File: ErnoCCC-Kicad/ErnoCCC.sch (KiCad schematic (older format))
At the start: 81 parts, among them J1 6VAC, J2 ICSP, J3 FTDI, J4 Erno Controller, J5 SWITCH, J6 LED OUT, J7 Conn_01x05, Q1 BC847, Q2 BC847, SW1 SW_Push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

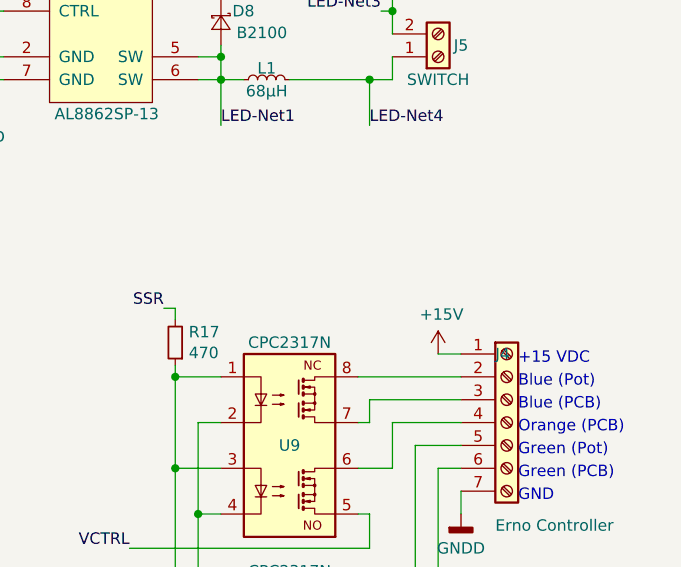
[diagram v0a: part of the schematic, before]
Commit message: Adding a 15VDC Elko
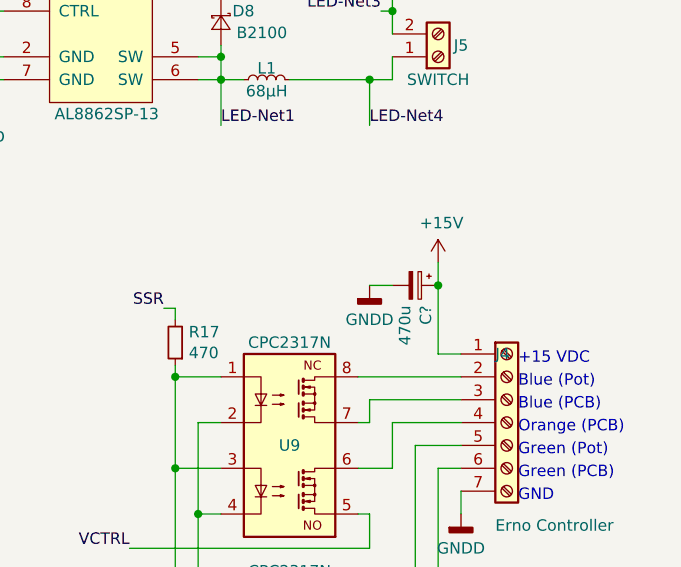
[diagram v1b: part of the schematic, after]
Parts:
- added C?: 470u, Capacitor_SMD:CP_Elec_10x10, symbol Device:CP_Small
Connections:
- wire segments 310 -> 313
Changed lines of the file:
@@
 Text Notes 10400 3850 0    50   ~ 0
 GND
-$Comp
-L power:+15V #PWR032
-U 1 1 5E443EB7
-P 10050 3200
-F 0 "#PWR032" H 10050 3050 50  0001 C CNN
-F 1 "+15V" H 10065 3373 50  0000 C CNN
-F 2 "" H 10050 3200 50  0001 C CNN
-F 3 "" H 10050 3200 50  0001 C CNN
-	1    10050 3200
-	1    0    0    -1
-$EndComp
 Text Notes 10400 3750 0    50   ~ 0
 Green (PCB)
@@
 Wire Wire Line
 	5600 4900 5700 4900
+$Comp
+L Device:CP_Small C?
+U 1 1 5E1CEF91
+P 9950 2900
+F 0 "C?" H 10038 2946 50  0000 L CNN
+F 1 "470u" H 10038 2855 50  0000 L CNN
+F 2 "Capacitor_SMD:CP_Elec_10x10" H 9950 2900 50  0001 C CNN
+F 3 "https://www.mouser.de/datasheet/2/293/e-wd-1511808.pdf" H 9950 2900 50  0001 C CNN
+	1    9950 2900
+	0    1    1    0
+$EndComp
+$Comp
+L power:+15V #PWR032
+U 1 1 5E443EB7
+P 10050 2800
+F 0 "#PWR032" H 10050 2650 50  0001 C CNN
+F 1 "+15V" H 10065 2973 50  0000 C CNN
+F 2 "" H 10050 2800 50  0001 C CNN
+F 3 "" H 10050 2800 50  0001 C CNN
+	1    10050 2800
+	1    0    0    -1
+$EndComp
+$Comp
+L power:GNDD #PWR?
+U 1 1 5E1D39DC
+P 9750 2900
+F 0 "#PWR?" H 9750 2650 50  0001 C CNN
+F 1 "GNDD" H 9750 2750 50  0000 C CNN
+F 2 "" H 9750 2900 50  0001 C CNN
+F 3 "" H 9750 2900 50  0001 C CNN
+	1    9750 2900
+	1    0    0    -1
+$EndComp
+Wire Wire Line
+	9750 2900 9850 2900
+Wire Wire Line
+	10050 2900 10050 3200
+Wire Wire Line
+	10050 2800 10050 2900
+Connection ~ 10050 2900
 $EndSCHEMATC

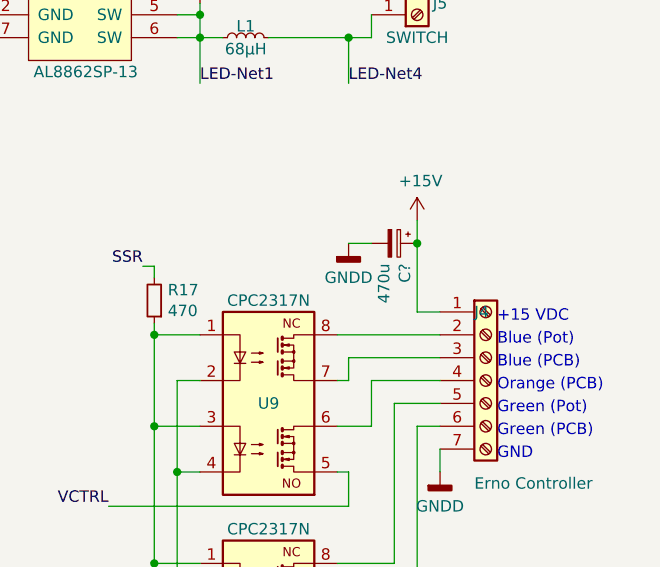
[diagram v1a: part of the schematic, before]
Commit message: Updating the Pin Header Length (6x done, 4x and 7x to follow)
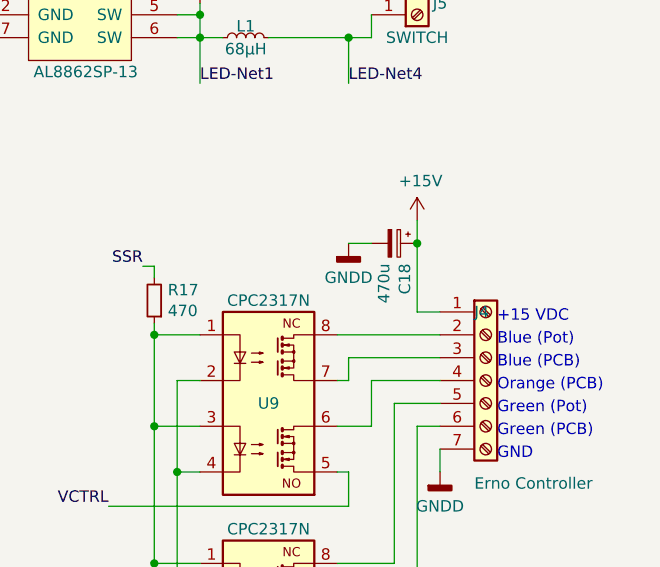
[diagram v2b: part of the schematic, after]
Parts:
- C12, C15: footprint Capacitor_SMD:CP_Elec_5x5.8 -> Capacitor_SMD:CP_Elec_4x4.5
- J3: footprint Connector_PinHeader_2.54mm:PinHeader_1x06_P2.54mm_Horizontal -> Connector_PinHeader_2.54mm:PinHeader_1x06_P2.54mm_Horizontal_shorter
- gave numbers to parts that had none: 1
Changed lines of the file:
@@
 F 0 "J3" H 4830 4592 50  0000 L CNN
 F 1 "FTDI" H 4750 4200 50  0000 L CNN
-F 2 "Connector_PinHeader_2.54mm:PinHeader_1x06_P2.54mm_Horizontal" H 4750 4600 50  0001 C CNN
+F 2 "Connector_PinHeader_2.54mm:PinHeader_1x06_P2.54mm_Horizontal_shorter" H 4750 4600 50  0001 C CNN
 F 3 "~" H 4750 4600 50  0001 C CNN
 	1    4750 4600
@@
 F 0 "C12" H 3050 1250 50  0000 L CNN
 F 1 "10u" H 3000 1050 50  0000 L CNN
-F 2 "Capacitor_SMD:CP_Elec_5x5.8" H 3200 1150 50  0001 C CNN
+F 2 "Capacitor_SMD:CP_Elec_4x4.5" H 3200 1150 50  0001 C CNN
 F 3 "https://www.mouser.de/datasheet/2/293/e-cd-1511557.pdf" H 3200 1150 50  0001 C CNN
 	1    3200 1150
@@
 F 0 "C15" V 8100 1500 50  0000 C CNN
 F 1 "10u" V 8050 1650 50  0000 C CNN
-F 2 "Capacitor_SMD:CP_Elec_5x5.8" H 7950 1550 50  0001 C CNN
+F 2 "Capacitor_SMD:CP_Elec_4x4.5" H 7950 1550 50  0001 C CNN
 F 3 "https://www.mouser.de/datasheet/2/293/e-cd-1511557.pdf" H 7950 1550 50  0001 C CNN
 	1    7950 1550
@@
 	5600 4900 5700 4900
 $Comp
-L Device:CP_Small C?
+L Device:CP_Small C18
 U 1 1 5E1CEF91
 P 9950 2900
-F 0 "C?" H 10038 2946 50  0000 L CNN
+F 0 "C18" H 10038 2946 50  0000 L CNN
 F 1 "470u" H 10038 2855 50  0000 L CNN
 F 2 "Capacitor_SMD:CP_Elec_10x10" H 9950 2900 50  0001 C CNN
@@
 $EndComp
 $Comp
-L power:GNDD #PWR?
+L power:GNDD #PWR034
 U 1 1 5E1D39DC
 P 9750 2900
-F 0 "#PWR?" H 9750 2650 50  0001 C CNN
+F 0 "#PWR034" H 9750 2650 50  0001 C CNN
 F 1 "GNDD" H 9750 2750 50  0000 C CNN
 F 2 "" H 9750 2900 50  0001 C CNN

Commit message: Fixing Schematics Bugs, PCB progress
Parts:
- D9: footprint Connector_PinHeader_2.54mm:PinHeader_1x04_P2.54mm_Horizontal -> Connector_PinHeader_2.54mm:PinHeader_1x04_P2.54mm_Horizontal_shorter
- J7: footprint Connector_PinHeader_2.54mm:PinHeader_1x05_P2.54mm_Horizontal -> Connector_PinHeader_2.54mm:PinHeader_1x05_P2.54mm_Horizontal_shorter
- U1, U2: footprint ErnoCCC:QRE1113GR -> ErnoCCC:QRE1113GR-slim
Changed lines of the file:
@@
 F 0 "U2" H 2050 7517 50  0000 C CNN
 F 1 "QRE1113" H 2050 7426 50  0000 C CNN
-F 2 "ErnoCCC:QRE1113GR" H 2050 7000 50  0001 C CNN
+F 2 "ErnoCCC:QRE1113GR-slim" H 2050 7000 50  0001 C CNN
 F 3 "http://www.onsemi.com/pub/Collateral/QRE1113-D.PDF" H 2050 7300 50  0001 C CNN
 	1    2050 7200
@@
 F 0 "U1" H 2050 6517 50  0000 C CNN
 F 1 "QRE1113" H 2050 6426 50  0000 C CNN
-F 2 "ErnoCCC:QRE1113GR" H 2050 6000 50  0001 C CNN
+F 2 "ErnoCCC:QRE1113GR-slim" H 2050 6000 50  0001 C CNN
 F 3 "http://www.onsemi.com/pub/Collateral/QRE1113-D.PDF" H 2050 6300 50  0001 C CNN
 	1    2050 6200
@@
 F 0 "D9" H 4900 3550 50  0000 L CNN
 F 1 "OLED 128x64" H 4700 2950 50  0000 L CNN
-F 2 "Connector_PinHeader_2.54mm:PinHeader_1x04_P2.54mm_Horizontal" H 4850 2950 50  0001 C CNN
+F 2 "Connector_PinHeader_2.54mm:PinHeader_1x04_P2.54mm_Horizontal_shorter" H 4850 2950 50  0001 C CNN
 F 3 "" H 4850 2950 50  0001 C CNN
 	1    4850 2950
@@
 F 0 "J7" H 5318 4375 50  0000 C CNN
 F 1 "Conn_01x05" H 5318 4466 50  0000 C CNN
-F 2 "Connector_PinHeader_2.54mm:PinHeader_1x05_P2.54mm_Horizontal" H 5400 4900 50  0001 C CNN
+F 2 "Connector_PinHeader_2.54mm:PinHeader_1x05_P2.54mm_Horizontal_shorter" H 5400 4900 50  0001 C CNN
 F 3 "~" H 5400 4900 50  0001 C CNN
 	1    5400 4900
@@
 	7050 3800 7050 3850
 Text Label 7500 3500 0    50   ~ 0
-VCTRL
+DAC
 Wire Wire Line
 	7450 3500 7500 3500

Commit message: Spreading out parts
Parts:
- removed TP4: GRAY-B, TestPoint:TestPoint_THTPad_D1.5mm_Drill0.7mm, symbol Connector:TestPoint
- removed TP5: GRAY-A, TestPoint:TestPoint_THTPad_D1.5mm_Drill0.7mm, symbol Connector:TestPoint
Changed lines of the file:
@@
 ICP1
-$Comp
-L Connector:TestPoint TP5
-U 1 1 5E1C35DB
-P 4450 7000
-F 0 "TP5" H 4400 7250 50  0000 L CNN
-F 1 "GRAY-A" H 4500 7150 50  0000 L CNN
-F 2 "TestPoint:TestPoint_THTPad_D1.5mm_Drill0.7mm" H 4650 7000 50  0001 C CNN
-F 3 "~" H 4650 7000 50  0001 C CNN
-	1    4450 7000
-	1    0    0    -1
-$EndComp
-$Comp
-L Connector:TestPoint TP4
-U 1 1 5E1C43D3
-P 4450 6000
-F 0 "TP4" H 4400 6250 50  0000 L CNN
-F 1 "GRAY-B" H 4500 6150 50  0000 L CNN
-F 2 "TestPoint:TestPoint_THTPad_D1.5mm_Drill0.7mm" H 4650 6000 50  0001 C CNN
-F 3 "~" H 4650 6000 50  0001 C CNN
-	1    4450 6000
-	1    0    0    -1
-$EndComp
 $Comp
 L Connector:TestPoint TP1
@@
 	1    0    0    -1
 $EndComp
-Connection ~ 4450 7000
 $Comp
 L 74xx:74HC14 U4

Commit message: Fixed Exe Distance, fixed Display Position, fixed missing i2c on DAC, added Diode to Motor Out, Added labels to pinouts, removed Peephole LED
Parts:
- removed D10: Peephole, LED_SMD:LED_0805_2012Metric_Castellated, symbol Device:LED_Small
- added D?: D_Schottky_Small, symbol Device:D_Schottky_Small
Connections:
- wire segments 313 -> 314
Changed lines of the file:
@@
 	1    0    0    -1
-$EndComp
-$Comp
-L Device:LED_Small D10
-U 1 1 602033E2
-P 5850 6000
-F 0 "D10" H 5650 6000 50  0000 C CNN
-F 1 "Peephole" H 5400 6000 50  0000 C CNN
-F 2 "LED_SMD:LED_0805_2012Metric_Castellated" V 5850 6000 50  0001 C CNN
-F 3 "~" V 5850 6000 50  0001 C CNN
-	1    5850 6000
-	-1   0    0    1
 $EndComp
 Wire Wire Line
@@
 L power:+5V #PWR025
 U 1 1 6022183D
-P 5700 6000
-F 0 "#PWR025" H 5700 5850 50  0001 C CNN
-F 1 "+5V" H 5750 6150 50  0000 C CNN
-F 2 "" H 5700 6000 50  0001 C CNN
-F 3 "" H 5700 6000 50  0001 C CNN
-	1    5700 6000
-	1    0    0    -1
-$EndComp
-Wire Wire Line
-	5700 6000 5750 6000
+P 5950 6000
+F 0 "#PWR025" H 5950 5850 50  0001 C CNN
+F 1 "+5V" H 6000 6150 50  0000 C CNN
+F 2 "" H 5950 6000 50  0001 C CNN
+F 3 "" H 5950 6000 50  0001 C CNN
+	1    5950 6000
+	1    0    0    -1
+$EndComp
 Wire Wire Line
 	900  1000 900  1250
@@
 	-1   0    0    1
 $EndComp
-Wire Wire Line
-	9700 5950 9750 5950
-Text Label 9750 5950 0    50   ~ 0
-VCTRL
 $Comp
 L power:GNDD #PWR022
@@
 	1    0    0    -1
 $EndComp
-Text Label 8700 4050 2    50   ~ 0
+Text Label 8450 4050 2    50   ~ 0
 VCTRL
 Wire Wire Line
@@
 Wire Wire Line
 	7300 3150 7500 3150
-$Comp
-L power:GNDD #PWR028
-U 1 1 5E2B49E3
-P 6650 3850
-F 0 "#PWR028" H 6650 3600 50  0001 C CNN
-F 1 "GNDD" H 6650 3700 50  0000 C CNN
-F 2 "" H 6650 3850 50  0001 C CNN
-F 3 "" H 6650 3850 50  0001 C CNN
-	1    6650 3850
-	1    0    0    -1
-$EndComp
-Wire Wire Line
-	6650 3600 6650 3850
 Wire Wire Line
 	5800 1050 5750 1050
@@
 	10050 2800 10050 2900
 Connection ~ 10050 2900
+Wire Wire Line
+	6650 3400 6600 3400
+Wire Wire Line
+	6650 3500 6600 3500
+$Comp
+L Device:D_Schottky_Small D?
+U 1 1 5E56B5CC
+P 8600 4050
+F 0 "D?" H 8600 4200 50  0000 C CNN
+F 1 "D_Schottky_Small" H 8600 3950 50  0000 C CNN
+F 2 "" V 8600 4050 50  0001 C CNN
+F 3 "~" V 8600 4050 50  0001 C CNN
+	1    8600 4050
+	1    0    0    -1
+$EndComp
+Wire Wire Line
+	8450 4050 8500 4050
+$Comp
+L power:GNDD #PWR028
+U 1 1 5E2B49E3
+P 6650 3850
+F 0 "#PWR028" H 6650 3600 50  0001 C CNN
+F 1 "GNDD" H 6650 3700 50  0000 C CNN
+F 2 "" H 6650 3850 50  0001 C CNN
+F 3 "" H 6650 3850 50  0001 C CNN
+	1    6650 3850
+	1    0    0    -1
+$EndComp
+Wire Wire Line
+	6650 3600 6650 3850
 $EndSCHEMATC

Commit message: Gute Nacht
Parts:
- D10: renamed from D?; footprint (none) -> Diode_SMD:D_SMB
- R15: value 27k -> 22k
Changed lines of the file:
@@
 P 5600 1350
 F 0 "R15" H 5750 1300 50  0000 C CNN
-F 1 "27k" H 5750 1400 50  0000 C CNN
+F 1 "22k" H 5750 1400 50  0000 C CNN
 F 2 "Resistor_SMD:R_0805_2012Metric" H 5600 1350 50  0001 C CNN
 F 3 "~" H 5600 1350 50  0001 C CNN
@@
 	6650 3500 6600 3500
 $Comp
-L Device:D_Schottky_Small D?
+L Device:D_Schottky_Small D10
 U 1 1 5E56B5CC
 P 8600 4050
-F 0 "D?" H 8600 4200 50  0000 C CNN
+F 0 "D10" H 8600 4200 50  0000 C CNN
 F 1 "D_Schottky_Small" H 8600 3950 50  0000 C CNN
-F 2 "" V 8600 4050 50  0001 C CNN
+F 2 "Diode_SMD:D_SMB" V 8600 4050 50  0001 C CNN
 F 3 "~" V 8600 4050 50  0001 C CNN
 	1    8600 4050
@@
 Wire Wire Line
 	6650 3600 6650 3850
+Text Label 5700 5200 0    50   ~ 0
+MOSI
+Text Label 5700 5300 0    50   ~ 0
+MISO
+Text Label 5700 5400 0    50   ~ 0
+SCK
 $EndSCHEMATC

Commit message: Updating Connectors for RevC
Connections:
- net labels added: A3
- net labels removed: D9
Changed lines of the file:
@@
 Text Label 2150 3500 0    50   ~ 0
 o
-Text Label 2150 3600 0    50   ~ 0
+Text Label 2150 2500 0    50   ~ 0
 >
 Text Label 2150 4800 0    50   ~ 0
@@
 Wire Wire Line
 	4500 7000 4500 7200
-Text Label 5700 5100 0    50   ~ 0
-GRAY-A
-Text Label 5700 5000 0    50   ~ 0
-GRAY-B
-Text Label 5700 4900 0    50   ~ 0
-SSR
 Wire Wire Line
 	5600 4700 5700 4700
@@
 Wire Wire Line
 	5800 1050 5750 1050
-Text Label 2150 2500 0    50   ~ 0
-D9
 Wire Wire Line
 	2000 2600 2150 2600
-Text Label 5700 4800 0    50   ~ 0
-D9
 Wire Wire Line
 	5600 4800 5700 4800
@@
 Wire Wire Line
 	6650 3600 6650 3850
-Text Label 5700 5200 0    50   ~ 0
+Text Label 5700 4900 0    50   ~ 0
 MOSI
-Text Label 5700 5300 0    50   ~ 0
+Text Label 5700 5000 0    50   ~ 0
 MISO
-Text Label 5700 5400 0    50   ~ 0
+Text Label 5700 5100 0    50   ~ 0
 SCK
+Text Label 2150 3600 0    50   ~ 0
+A3
+Text Label 5700 4800 0    50   ~ 0
+A3
 $EndSCHEMATC

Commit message: Adding all the Improvements: SPI, TPs for DAV, VCTRL, SSR, GRAY. Also, GND and VCC on J7
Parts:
- added TP4: VCTRL, TestPoint:TestPoint_THTPad_1.5x1.5mm_Drill0.7mm, symbol Connector:TestPoint
- added TP5: DAC, TestPoint:TestPoint_THTPad_1.5x1.5mm_Drill0.7mm, symbol Connector:TestPoint
- added TP6, TP8: GRAY-B, TestPoint:TestPoint_THTPad_1.5x1.5mm_Drill0.7mm, symbol Connector:TestPoint
- added TP7: GRAY-A, TestPoint:TestPoint_THTPad_1.5x1.5mm_Drill0.7mm, symbol Connector:TestPoint
- J7: value Conn_01x05 -> Conn_01x07; symbol Connector_Generic:Conn_01x05 -> Connector_Generic:Conn_01x07
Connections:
- wire segments 314 -> 325
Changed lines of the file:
@@
 Connection ~ 2350 5700
 Connection ~ 2350 6100
-Text Label 4500 7000 0    50   ~ 0
+Text Label 4550 7000 0    50   ~ 0
 INT0
 Text Label 4500 6000 0    50   ~ 0
@@
 Wire Wire Line
 	4450 6000 4500 6000
-Text Label 4500 7100 0    50   ~ 0
+Text Label 4550 7100 0    50   ~ 0
 ICP1
 $Comp
@@
 D10
 $Comp
-L Connector_Generic:Conn_01x05 J7
+L Connector_Generic:Conn_01x07 J7
 U 1 1 5E107107
 P 5400 4900
 F 0 "J7" H 5318 4375 50  0000 C CNN
-F 1 "Conn_01x05" H 5318 4466 50  0000 C CNN
+F 1 "Conn_01x07" H 5318 4466 50  0000 C CNN
 F 2 "Connector_PinHeader_2.54mm:PinHeader_1x05_P2.54mm_Horizontal_shorter" H 5400 4900 50  0001 C CNN
 F 3 "~" H 5400 4900 50  0001 C CNN
@@
 Text Label 5700 4700 0    50   ~ 0
 D10
-Text Label 4500 7200 0    50   ~ 0
+Text Label 4550 7200 0    50   ~ 0
 GRAY-A
 Text Label 4500 6100 0    50   ~ 0
@@
 Wire Wire Line
 	4450 6100 4500 6100
-Wire Wire Line
-	4500 7000 4500 7200
 Wire Wire Line
 	5600 4700 5700 4700
@@
 Text Label 5700 4800 0    50   ~ 0
 A3
+$Comp
+L Connector:TestPoint TP5
+U 1 1 5E55D944
+P 7500 3600
+F 0 "TP5" V 7454 3788 50  0000 L CNN
+F 1 "DAC" V 7545 3788 50  0000 L CNN
+F 2 "TestPoint:TestPoint_THTPad_1.5x1.5mm_Drill0.7mm" H 7700 3600 50  0001 C CNN
+F 3 "~" H 7700 3600 50  0001 C CNN
+	1    7500 3600
+	0    1    1    0
+$EndComp
+Wire Wire Line
+	7500 3600 7500 3500
+$Comp
+L Connector:TestPoint TP4
+U 1 1 5E5787D7
+P 6750 1250
+F 0 "TP4" V 6704 1438 50  0000 L CNN
+F 1 "VCTRL" V 6795 1438 50  0000 L CNN
+F 2 "TestPoint:TestPoint_THTPad_1.5x1.5mm_Drill0.7mm" H 6950 1250 50  0001 C CNN
+F 3 "~" H 6950 1250 50  0001 C CNN
+	1    6750 1250
+	0    1    1    0
+$EndComp
+Wire Wire Line
+	6750 1150 6750 1250
+Text Label 5700 4600 0    50   ~ 0
+5V
+Text Label 5700 5200 0    50   ~ 0
+GNDD
+Wire Wire Line
+	5600 4600 5700 4600
+Wire Wire Line
+	5600 5200 5700 5200
+$Comp
+L Connector:TestPoint TP7
+U 1 1 5E645CBA
+P 4500 7300
+F 0 "TP7" V 4600 7300 50  0000 L CNN
+F 1 "GRAY-A" V 4500 7500 50  0000 L CNN
+F 2 "TestPoint:TestPoint_THTPad_1.5x1.5mm_Drill0.7mm" H 4700 7300 50  0001 C CNN
+F 3 "~" H 4700 7300 50  0001 C CNN
+	1    4500 7300
+	0    1    1    0
+$EndComp
+$Comp
+L Connector:TestPoint TP6
+U 1 1 5E646616
+P 4450 6200
+F 0 "TP6" V 4550 6200 50  0000 L CNN
+F 1 "GRAY-B" V 4450 6400 50  0000 L CNN
+F 2 "TestPoint:TestPoint_THTPad_1.5x1.5mm_Drill0.7mm" H 4650 6200 50  0001 C CNN
+F 3 "~" H 4650 6200 50  0001 C CNN
+	1    4450 6200
+	0    1    1    0
+$EndComp
+Wire Wire Line
+	4500 7000 4500 7100
+Wire Wire Line
+	4450 6100 4450 6200
+Connection ~ 4450 6100
+Wire Wire Line
+	4550 7000 4500 7000
+Connection ~ 4500 7000
+Wire Wire Line
+	4550 7100 4500 7100
+Connection ~ 4500 7100
+Wire Wire Line
+	4500 7100 4500 7200
+Wire Wire Line
+	4550 7200 4500 7200
+Connection ~ 4500 7200
+Wire Wire Line
+	4500 7200 4500 7300
+$Comp
+L Connector:TestPoint TP8
+U 1 1 5E6E25FF
+P 8900 2900
+F 0 "TP8" V 8800 2950 50  0000 L CNN
+F 1 "GRAY-B" V 8900 3100 50  0000 L CNN
+F 2 "TestPoint:TestPoint_THTPad_1.5x1.5mm_Drill0.7mm" H 9100 2900 50  0001 C CNN
+F 3 "~" H 9100 2900 50  0001 C CNN
+	1    8900 2900
+	0    1    1    0
+$EndComp
+Wire Wire Line
+	8900 2900 8900 3000
+Connection ~ 8900 3000
 $EndSCHEMATC
